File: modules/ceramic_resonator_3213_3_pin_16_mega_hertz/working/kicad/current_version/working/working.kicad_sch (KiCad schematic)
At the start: 3 parts, among them x1 xcr3213mhz16

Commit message: a few module workings
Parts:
- removed C1, C2: c6pf22, c6pf22_electronic_capacitor_0603_22_pico_farad, symbol oomlout_oomp_part_symbols:c6pf22_electronic_capacitor_0603_22_pico_farad
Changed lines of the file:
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@@
 (kicad_sch (version 20230121) (generator eeschema)
   (paper "A4")
-  (junction (at 140.97 87.63) (diameter 0) (color 0 0 0 0)
-  )
-  (junction (at 151.13 76.2) (diameter 0) (color 0 0 0 0)
-  )
-  (junction (at 130.81 76.2) (diameter 0) (color 0 0 0 0)
-  )
-  (wire (pts (xy 130.81 87.63) (xy 140.97 87.63))
-    (stroke (width 0) (type default))
-  )
-  (wire (pts (xy 151.13 87.63) (xy 151.13 86.36))
-    (stroke (width 0) (type default))
-  )
-  (wire (pts (xy 140.97 87.63) (xy 151.13 87.63))
-    (stroke (width 0) (type default))
-  )
-  (wire (pts (xy 130.81 86.36) (xy 130.81 87.63))
-    (stroke (width 0) (type default))
-  )
   (wire (pts (xy 140.97 81.28) (xy 140.97 87.63))
     (stroke (width 0) (type default))
   )
-  (wire (pts (xy 151.13 76.2) (xy 151.13 78.74))
+  (wire (pts (xy 128.27 76.2) (xy 137.16 76.2))
     (stroke (width 0) (type default))
   )
-  (wire (pts (xy 128.27 76.2) (xy 130.81 76.2))
-    (stroke (width 0) (type default))
-  )
-  (wire (pts (xy 130.81 76.2) (xy 137.16 76.2))
-    (stroke (width 0) (type default))
-  )
-  (wire (pts (xy 130.81 76.2) (xy 130.81 78.74))
-    (stroke (width 0) (type default))
-  )
-  (wire (pts (xy 151.13 76.2) (xy 153.67 76.2))
-    (stroke (width 0) (type default))
-  )
-  (wire (pts (xy 144.78 76.2) (xy 151.13 76.2))
+  (wire (pts (xy 144.78 76.2) (xy 153.67 76.2))
     (stroke (width 0) (type default))
   )
@@
     (effects (font (size 1.27 1.27)) (justify right bottom))
   )
-  (symbol (lib_id "oomlout_oomp_part_symbols:c6pf22_electronic_capacitor_0603_22_pico_farad") (at 130.81 82.55 0) (unit 1)
-    (in_bom yes) (on_board yes) (dnp no)
-    (property "Reference" "C1" (at 124.46 81.28 0)
-      (effects (font (size 1.27 1.27)) (justify left))
-    )
-    (property "Value" "c6pf22" (at 120.65 83.82 0)
-      (effects (font (size 1.27 1.27)) (justify left))
-    )
-    (property "Footprint" "c6pf22_electronic_capacitor_0603_22_pico_farad" (at 131.7752 86.36 0)
-      (effects (font (size 1.27 1.27)) hide)
-    )
-    (property "Datasheet" "https://github.com/oomlout/oomlout_oomp_v3/parts/electronic_capacitor_0603_22_pico_farad/datasheet.pdf" (at 130.81 82.55 0)
-      (effects (font (size 1.27 1.27)) hide)
-    )
-    (pin "1")
-    (pin "2")
-    (instances
-      (project "working"
-        (path "/3a6aff3f-64f2-4c1e-bb10-1dc442a40a0c"
-          (reference "C1") (unit 1)
-        )
-      )
-    )
-  )
   (symbol (lib_id "oomlout_oomp_part_symbols:xcr3213mhz16_electronic_ceramic_resonator_3213_3_pin_ground_pin_2_16_mega_hertz") (at 140.97 76.2 0) (unit 1)
     (in_bom yes) (on_board yes) (dnp no) (fields_autoplaced)
@@
         )
       )
-    )
-  )
-  (symbol (lib_id "oomlout_oomp_part_symbols:c6pf22_electronic_capacitor_0603_22_pico_farad") (at 151.13 82.55 0) (unit 1)
-    (in_bom yes) (on_board yes) (dnp no)
-    (property "Reference" "C2" (at 154.94 81.28 0)
-      (effects (font (size 1.27 1.27)) (justify left))
-    )
-    (property "Value" "c6pf22" (at 154.94 83.82 0)
-      (effects (font (size 1.27 1.27)) (justify left))
-    )
-    (property "Footprint" "c6pf22_electronic_capacitor_0603_22_pico_farad" (at 152.0952 86.36 0)
-      (effects (font (size 1.27 1.27)) hide)
-    )
-    (property "Datasheet" "https://github.com/oomlout/oomlout_oomp_v3/parts/electronic_capacitor_0603_22_pico_farad/datasheet.pdf" (at 151.13 82.55 0)
-      (effects (font (size 1.27 1.27)) hide)
-    )
-    (pin "1")
-    (pin "2")
-    (instances
-      (project "working"
-        (path "/3a6aff3f-64f2-4c1e-bb10-1dc442a40a0c"
-          (reference "C2") (unit 1)
-        )
-      )

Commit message: a few module fixes
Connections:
- net xtal_1 renamed xtal1
- net xtal_2 renamed xtal2
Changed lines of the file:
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@@
     (effects (font (size 4 4) (thickness 0.8) bold (color 255 255 255 1)) (justify right bottom))
   )
-  (label "xtal_2" (at 153.67 76.2 0) (fields_autoplaced)
+  (label "xtal2" (at 153.67 76.2 0) (fields_autoplaced)
     (effects (font (size 1.27 1.27)) (justify left bottom))
   )
-  (label "xtal_1" (at 128.27 76.2 180) (fields_autoplaced)
+  (label "xtal1" (at 128.27 76.2 180) (fields_autoplaced)
     (effects (font (size 1.27 1.27)) (justify right bottom))
   )

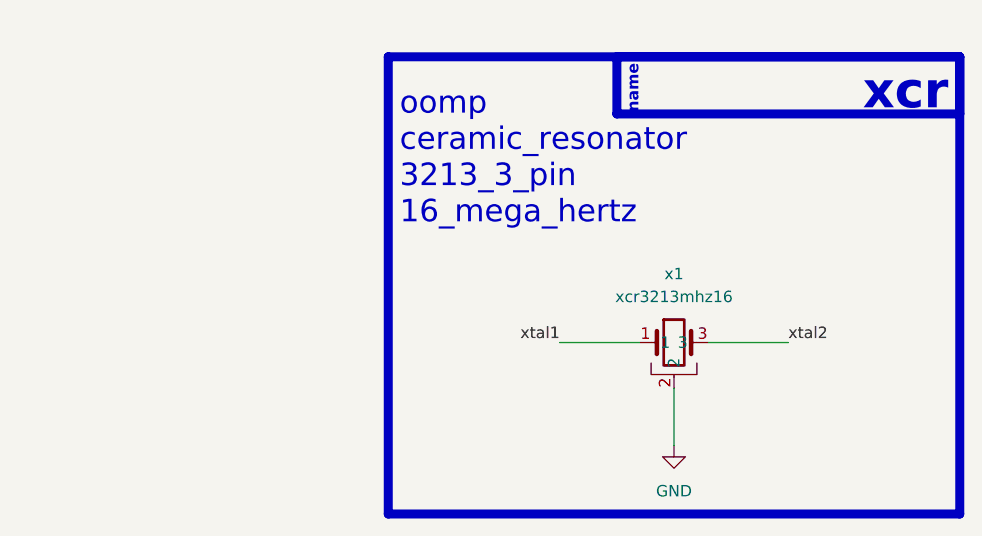
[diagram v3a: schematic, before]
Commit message: fixed formatting to be more consistent
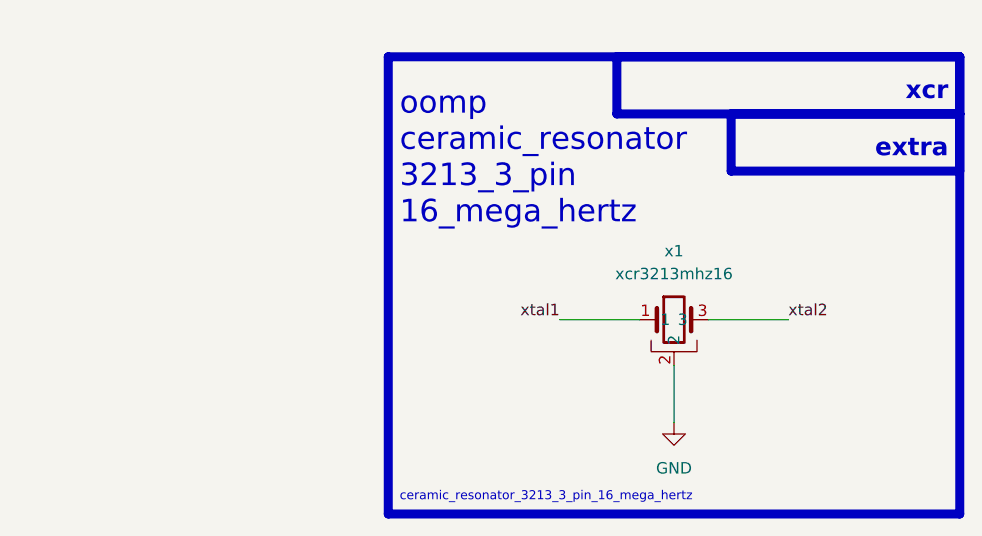
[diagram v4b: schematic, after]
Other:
- note added: "ceramic_resonator_3213_3_pin_16_mega_hertz"
- note added: "extra"
- note removed: "name"
- moved on the sheet: x1
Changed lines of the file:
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@@
 (kicad_sch (version 20230121) (generator eeschema)
   (paper "A4")
-  (wire (pts (xy 140.97 81.28) (xy 140.97 87.63))
+  (wire (pts (xy 140.97 78.74) (xy 140.97 85.09))
     (stroke (width 0) (type default))
   )
-  (wire (pts (xy 128.27 76.2) (xy 137.16 76.2))
+  (wire (pts (xy 128.27 73.66) (xy 137.16 73.66))
     (stroke (width 0) (type default))
   )
-  (wire (pts (xy 144.78 76.2) (xy 153.67 76.2))
+  (wire (pts (xy 144.78 73.66) (xy 153.67 73.66))
     (stroke (width 0) (type default))
   )
@@
     (fill (type none))
   )
+  (rectangle (start 147.32 50.8) (end 172.72 57.15)
+    (stroke (width 1) (type default))
+    (fill (type none))
+  )
   (rectangle (start 134.62 44.45) (end 172.72 50.8)
     (stroke (width 1) (type default))
-    (fill (type color) (color 0 0 0 0))
+    (fill (type none))
   )
   (rectangle (start 109.22 44.45) (end 172.72 95.25)
@@
     (fill (type none))
   )
-  (text "name" (at 137.16 50.8 90)
-    (effects (font (size 1.27 1.27) (thickness 0.254) bold (color 255 255 255 1)) (justify left bottom))
+  (text "extra" (at 171.45 55.88 0)
+    (effects (font (size 2 2) (thickness 0.8) bold) (justify right bottom))
   )
   (text "oomp\nceramic_resonator\n3213_3_pin\n16_mega_hertz\n\n" (at 110.49 67.31 0)
     (effects (font (size 2.5 2.5)) (justify left bottom))
   )
-  (text "xcr" (at 171.45 50.8 0)
-    (effects (font (size 4 4) (thickness 0.8) bold (color 255 255 255 1)) (justify right bottom))
+  (text "xcr" (at 171.45 49.53 0)
+    (effects (font (size 2 2) (thickness 0.8) bold) (justify right bottom))
   )
-  (label "xtal2" (at 153.67 76.2 0) (fields_autoplaced)
+  (text "ceramic_resonator_3213_3_pin_16_mega_hertz" (at 110.49 93.98 0)
+    (effects (font (size 1 1)) (justify left bottom))
+  )
+  (label "xtal2" (at 153.67 73.66 0) (fields_autoplaced)
     (effects (font (size 1.27 1.27)) (justify left bottom))
   )
-  (label "xtal1" (at 128.27 76.2 180) (fields_autoplaced)
+  (label "xtal1" (at 128.27 73.66 180) (fields_autoplaced)
     (effects (font (size 1.27 1.27)) (justify right bottom))
   )
-  (symbol (lib_id "oomlout_oomp_part_symbols:xcr3213mhz16_electronic_ceramic_resonator_3213_3_pin_ground_pin_2_16_mega_hertz") (at 140.97 76.2 0) (unit 1)
+  (symbol (lib_id "oomlout_oomp_part_symbols:xcr3213mhz16_electronic_ceramic_resonator_3213_3_pin_ground_pin_2_16_mega_hertz") (at 140.97 73.66 0) (unit 1)
     (in_bom yes) (on_board yes) (dnp no) (fields_autoplaced)
-    (property "Reference" "x1" (at 140.97 68.58 0)
+    (property "Reference" "x1" (at 140.97 66.04 0)
       (effects (font (size 1.27 1.27)))
     )
-    (property "Value" "xcr3213mhz16" (at 140.97 71.12 0)
+    (property "Value" "xcr3213mhz16" (at 140.97 68.58 0)
       (effects (font (size 1.27 1.27)))
     )
-    (property "Footprint" "xcr3213mhz16_electronic_ceramic_resonator_3213_3_pin_ground_pin_2_16_mega_hertz" (at 140.97 76.2 0)
+    (property "Footprint" "xcr3213mhz16_electronic_ceramic_resonator_3213_3_pin_ground_pin_2_16_mega_hertz" (at 140.97 73.66 0)
       (effects (font (size 1.27 1.27)) hide)
     )
-    (property "Datasheet" "https://github.com/oomlout/oomlout_oomp_v3/parts/electronic_ceramic_resonator_3213_3_pin_ground_pin_2_16_mega_hertz/datasheet.pdf" (at 140.97 76.2 0)
+    (property "Datasheet" "https://github.com/oomlout/oomlout_oomp_v3/parts/electronic_ceramic_resonator_3213_3_pin_ground_pin_2_16_mega_hertz/datasheet.pdf" (at 140.97 73.66 0)
       (effects (font (size 1.27 1.27)) hide)
     )
@@
     )
   )
-  (symbol (lib_id "power:GND") (at 140.97 87.63 0) (unit 1)
+  (symbol (lib_id "power:GND") (at 140.97 85.09 0) (unit 1)
     (in_bom yes) (on_board yes) (dnp no) (fields_autoplaced)
-    (property "Reference" "#PWR02" (at 140.97 93.98 0)
+    (property "Reference" "#PWR02" (at 140.97 91.44 0)
       (effects (font (size 1.27 1.27)) hide)
     )
-    (property "Value" "GND" (at 140.97 92.71 0)
+    (property "Value" "GND" (at 140.97 90.17 0)
       (effects (font (size 1.27 1.27)))
     )
-    (property "Footprint" "" (at 140.97 87.63 0)
+    (property "Footprint" "" (at 140.97 85.09 0)
       (effects (font (size 1.27 1.27)) hide)
     )
-    (property "Datasheet" "" (at 140.97 87.63 0)
+    (property "Datasheet" "" (at 140.97 85.09 0)
       (effects (font (size 1.27 1.27)) hide)
     )

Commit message: schematic formatting
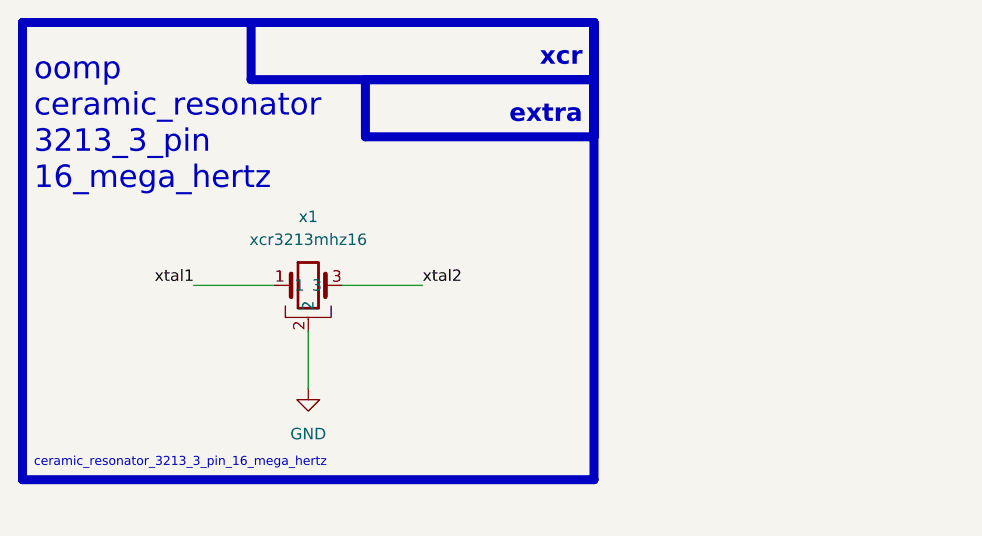
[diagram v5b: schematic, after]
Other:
- moved on the sheet: x1
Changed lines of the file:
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@@
 (kicad_sch (version 20230121) (generator eeschema)
-  (paper "A4")
-  (wire (pts (xy 140.97 78.74) (xy 140.97 85.09))
+  (paper "A5")
+  (wire (pts (xy 100.33 74.93) (xy 100.33 81.28))
     (stroke (width 0) (type default))
   )
-  (wire (pts (xy 128.27 73.66) (xy 137.16 73.66))
+  (wire (pts (xy 87.63 69.85) (xy 96.52 69.85))
     (stroke (width 0) (type default))
   )
-  (wire (pts (xy 144.78 73.66) (xy 153.67 73.66))
+  (wire (pts (xy 104.14 69.85) (xy 113.03 69.85))
     (stroke (width 0) (type default))
   )
-  (rectangle (start 171.45 101.6) (end 171.45 101.6)
+  (rectangle (start 130.81 97.79) (end 130.81 97.79)
     (stroke (width 0) (type default))
     (fill (type none))
   )
-  (rectangle (start 147.32 50.8) (end 172.72 57.15)
+  (rectangle (start 106.68 46.99) (end 132.08 53.34)
     (stroke (width 1) (type default))
     (fill (type none))
   )
-  (rectangle (start 134.62 44.45) (end 172.72 50.8)
+  (rectangle (start 93.98 40.64) (end 132.08 46.99)
     (stroke (width 1) (type default))
     (fill (type none))
   )
-  (rectangle (start 109.22 44.45) (end 172.72 95.25)
+  (rectangle (start 68.58 40.64) (end 132.08 91.44)
     (stroke (width 1) (type default))
     (fill (type none))
   )
-  (text "extra" (at 171.45 55.88 0)
+  (text "extra" (at 130.81 52.07 0)
     (effects (font (size 2 2) (thickness 0.8) bold) (justify right bottom))
   )
-  (text "oomp\nceramic_resonator\n3213_3_pin\n16_mega_hertz\n\n" (at 110.49 67.31 0)
+  (text "oomp\nceramic_resonator\n3213_3_pin\n16_mega_hertz\n\n" (at 69.85 63.5 0)
     (effects (font (size 2.5 2.5)) (justify left bottom))
   )
-  (text "xcr" (at 171.45 49.53 0)
+  (text "xcr" (at 130.81 45.72 0)
     (effects (font (size 2 2) (thickness 0.8) bold) (justify right bottom))
   )
-  (text "ceramic_resonator_3213_3_pin_16_mega_hertz" (at 110.49 93.98 0)
+  (text "ceramic_resonator_3213_3_pin_16_mega_hertz" (at 69.85 90.17 0)
     (effects (font (size 1 1)) (justify left bottom))
   )
-  (label "xtal2" (at 153.67 73.66 0) (fields_autoplaced)
+  (label "xtal2" (at 113.03 69.85 0) (fields_autoplaced)
     (effects (font (size 1.27 1.27)) (justify left bottom))
   )
-  (label "xtal1" (at 128.27 73.66 180) (fields_autoplaced)
+  (label "xtal1" (at 87.63 69.85 180) (fields_autoplaced)
     (effects (font (size 1.27 1.27)) (justify right bottom))
   )
-  (symbol (lib_id "oomlout_oomp_part_symbols:xcr3213mhz16_electronic_ceramic_resonator_3213_3_pin_ground_pin_2_16_mega_hertz") (at 140.97 73.66 0) (unit 1)
+  (symbol (lib_id "oomlout_oomp_part_symbols:xcr3213mhz16_electronic_ceramic_resonator_3213_3_pin_ground_pin_2_16_mega_hertz") (at 100.33 69.85 0) (unit 1)
     (in_bom yes) (on_board yes) (dnp no) (fields_autoplaced)
-    (property "Reference" "x1" (at 140.97 66.04 0)
+    (property "Reference" "x1" (at 100.33 62.23 0)
       (effects (font (size 1.27 1.27)))
     )
-    (property "Value" "xcr3213mhz16" (at 140.97 68.58 0)
+    (property "Value" "xcr3213mhz16" (at 100.33 64.77 0)
       (effects (font (size 1.27 1.27)))
     )
-    (property "Footprint" "xcr3213mhz16_electronic_ceramic_resonator_3213_3_pin_ground_pin_2_16_mega_hertz" (at 140.97 73.66 0)
+    (property "Footprint" "xcr3213mhz16_electronic_ceramic_resonator_3213_3_pin_ground_pin_2_16_mega_hertz" (at 100.33 69.85 0)
       (effects (font (size 1.27 1.27)) hide)
     )
-    (property "Datasheet" "https://github.com/oomlout/oomlout_oomp_v3/parts/electronic_ceramic_resonator_3213_3_pin_ground_pin_2_16_mega_hertz/datasheet.pdf" (at 140.97 73.66 0)
+    (property "Datasheet" "https://github.com/oomlout/oomlout_oomp_v3/parts/electronic_ceramic_resonator_3213_3_pin_ground_pin_2_16_mega_hertz/datasheet.pdf" (at 100.33 69.85 0)
       (effects (font (size 1.27 1.27)) hide)
     )
@@
     )
   )
-  (symbol (lib_id "power:GND") (at 140.97 85.09 0) (unit 1)
+  (symbol (lib_id "power:GND") (at 100.33 81.28 0) (unit 1)
     (in_bom yes) (on_board yes) (dnp no) (fields_autoplaced)
-    (property "Reference" "#PWR02" (at 140.97 91.44 0)
+    (property "Reference" "#PWR02" (at 100.33 87.63 0)
       (effects (font (size 1.27 1.27)) hide)
     )
-    (property "Value" "GND" (at 140.97 90.17 0)
+    (property "Value" "GND" (at 100.33 86.36 0)
       (effects (font (size 1.27 1.27)))
     )
-    (property "Footprint" "" (at 140.97 85.09 0)
+    (property "Footprint" "" (at 100.33 81.28 0)
       (effects (font (size 1.27 1.27)) hide)
     )
-    (property "Datasheet" "" (at 140.97 85.09 0)
+    (property "Datasheet" "" (at 100.33 81.28 0)
       (effects (font (size 1.27 1.27)) hide)
     )
